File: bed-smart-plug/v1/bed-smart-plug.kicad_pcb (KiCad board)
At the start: 2 copper layers, 122.6 x 80.6 mm, 26 parts, among them J1 DS18b20, J2 Conn_01x02_Male, J3 3.5mm headphone jack, J4 Triac gate protection, J5 Opto snubber, J6 Opto snubber 2, J7 Main, J8 Triac snubber, J9 Prises, Q1 BT136-600E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

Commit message: wip pcb v1
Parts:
- removed AE1: Antenna, Connector_PinHeader_2.54mm:PinHeader_1x01_P2.54mm_Vertical
- removed C1: 47nF/400V, Capacitor_SMD:C_1206_3216Metric
- removed C2: 10nF/400V, Capacitor_SMD:C_0805_2012Metric
- removed D1: LED, Diode_SMD:D_0805_2012Metric
- removed F1: 3A, Fuse:Fuseholder_Cylinder-5x20mm_Schurter_0031_8201_Horizontal_Open
- removed J1: DS18b20, Connector_PinHeader_2.54mm:PinHeader_1x03_P2.54mm_Vertical
- removed J2: Conn_01x02_Male, Connector_PinHeader_2.54mm:PinHeader_1x04_P2.54mm_Vertical
- removed J4: Triac gate protection, Connector_PinHeader_2.54mm:PinHeader_1x02_P2.54mm_Vertical
- removed J5: Opto snubber, Connector_PinHeader_2.54mm:PinHeader_1x03_P2.54mm_Vertical
- removed J6: Opto snubber 2, Connector_PinHeader_2.54mm:PinHeader_1x02_P2.54mm_Vertical
- removed J7: Main, TerminalBlock:TerminalBlock_bornier-2_P5.08mm
- removed J8: Triac snubber, Connector_PinHeader_2.54mm:PinHeader_1x02_P2.54mm_Vertical
- removed J9: Prises, TerminalBlock:TerminalBlock_bornier-2_P5.08mm
- removed PS1: Alim RS PRO 5V 1A, Converter_ACDC:Converter_ACDC_MeanWell_IRM-03-xx_THT
- removed R1: 4.7KΩ, Resistor_SMD:R_0402_1005Metric
- removed R2, R3: 220Ω, Resistor_SMD:R_0603_1608Metric
- removed R4: 360Ω/0.5W, Resistor_SMD:R_1210_3225Metric
- removed R5: 470Ω/0.5W, Resistor_SMD:R_1210_3225Metric
- removed R6: 39Ω/0.5W, Resistor_SMD:R_1210_3225Metric
- removed U2: AM-RX12A-433P, mylife-footprints:AMRX12A433P
- removed U3: MOC3021M, Package_DIP:SMDIP-6_W9.53mm
- added ?: , , F.Cu at (202.0, 57.2)
- added ?: , , F.Cu at (163.5, 83.7)
- added ?: , , F.Cu at (87.2, 57.2)
- added ?: , , F.Cu at (163.5, 55.8)
- added ?: , , F.Cu at (202.0, 111.4)
- moved J3 105.6 mm to (210.3, 78.6), turned to 180 degrees
- moved Q1 55.0 mm to (102.8, 68.5), turned to 90 degrees
- moved HS1 49.3 mm to (99.3, 65.9), turned to 90 degrees
- moved U1 44.3 mm to (179.9, 69.7), turned to 90 degrees
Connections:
- Q1 pad 1: Net-(J8-Pin_2) -> (no net)
- Q1 pad 2: Net-(J5-Pin_3) -> (no net)
- Q1 pad 3: Net-(Q1-G) -> (no net)
- U1 pad 1: +5V -> (no net)
- U1 pad 11: Net-(J1-Pin_3) -> (no net)
- U1 pad 19: Net-(U1-GPIO36) -> (no net)
- U1 pad 2: +3V3 -> (no net)
- U1 pad 3: GND -> (no net)
- U1 pad 7: Net-(U1-GPIO2) -> (no net)
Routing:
- net GND: track 189.9 -> 0.00 mm
- net +3V3: track 134.3 -> 0.00 mm, vias 1 -> 0
- net NEUT: track 97.6 -> 0.00 mm
- net Net-(U1-GPIO2): track 93.8 -> 0.00 mm
- net +5V: track 81.2 -> 0.00 mm
- net Net-(J5-Pin_3): track 78.1 -> 0.00 mm
- net LINE: track 63.4 -> 0.00 mm
- net Net-(J8-Pin_2): track 62.5 -> 0.00 mm
- net Net-(Q1-G): track 47.7 -> 0.00 mm
- net Net-(U1-GPIO36): track 34.1 -> 0.00 mm, vias 1 -> 0
- net Net-(J4-Pin_2): track 32.1 -> 0.00 mm
- net Net-(J4-Pin_1): track 28.5 -> 0.00 mm
- net Net-(J1-Pin_3): track 26.6 -> 0.00 mm
- net Net-(J5-Pin_1): track 21.9 -> 0.00 mm
- net Net-(R3-Pad1): track 20.2 -> 0.00 mm, vias 2 -> 0
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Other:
- board size 122.6 x 80.6 mm -> 145 x 75 mm
- board text removed: "3V3"
- board text removed: "Close x2=ON"
- board text removed: "Close=OFF"
- board text removed: "Close=ON"
- board text removed: "DATA"
- board text removed: "GND"
- board text removed: "Open=ON"

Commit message: wip pcb v1
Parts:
- added AE1: Antenna, Connector_PinHeader_2.54mm:PinHeader_1x01_P2.54mm_Vertical, F.Cu at (126.3, 136.2)
- added D1: LED, Diode_SMD:D_0805_2012Metric, F.Cu at (126.3, 140.1)
- added D2: LED, Diode_SMD:D_0805_2012Metric, F.Cu at (126.3, 143.1)
- added D3: LED, Diode_SMD:D_0805_2012Metric, F.Cu at (126.3, 146.2)
- added D4: LED, Diode_SMD:D_0805_2012Metric, F.Cu at (126.3, 149.2)
- added F1: 3A, Fuse:Fuseholder_Cylinder-5x20mm_Schurter_0031_8201_Horizontal_Open, F.Cu at (189.3, 90.5)
- added HS2: Heatsink (shared by 2 triacs), Heatsink:Heatsink_Fischer_SK104-STC-STIC_35x13mm_2xDrill2.5mm, F.Cu at (79.0, 69.4)
- added J2: Main + Sorties, TerminalBlock:TerminalBlock_bornier-6_P5.08mm, F.Cu at (132.5, 51.2)
- added PS1: Alim RS PRO 5V 1A, Converter_ACDC:Converter_ACDC_MeanWell_IRM-03-xx_THT, F.Cu at (107.9, 54.5)
- added Q2: BT136-600E, Package_TO_SOT_THT:TO-220-3_Vertical, F.Cu at (100.5, 71.8)
- added Q3: BT136-600E, Package_TO_SOT_THT:TO-220-3_Vertical, F.Cu at (113.6, 125.9)
- added Q4: BT136-600E, Package_TO_SOT_THT:TO-220-3_Vertical, F.Cu at (113.6, 131.9)
- added R1: 4.7KΩ, Resistor_SMD:R_0402_1005Metric, F.Cu at (125.5, 151.7)
- added R10: 220Ω, Resistor_SMD:R_0603_1608Metric, F.Cu at (116.4, 140.2)
- added R11: 220Ω, Resistor_SMD:R_0603_1608Metric, F.Cu at (116.4, 142.7)
- added R12: 220Ω, Resistor_SMD:R_0603_1608Metric, F.Cu at (116.4, 145.2)
- added R13: 360Ω/0.5W, Resistor_SMD:R_1210_3225Metric, F.Cu at (121.2, 136.0)
- added R14: 360Ω/0.5W, Resistor_SMD:R_1210_3225Metric, F.Cu at (121.2, 140.2)
- added R15: 360Ω/0.5W, Resistor_SMD:R_1210_3225Metric, F.Cu at (121.2, 144.4)
- added R16: 360Ω/0.5W, Resistor_SMD:R_1210_3225Metric, F.Cu at (121.2, 148.6)
- added R2: 10KΩ, Resistor_SMD:R_0603_1608Metric, F.Cu at (112.4, 135.2)
- added R3: 10KΩ, Resistor_SMD:R_0603_1608Metric, F.Cu at (112.4, 137.7)
- added R4: 10KΩ, Resistor_SMD:R_0603_1608Metric, F.Cu at (112.4, 140.2)
- added R5: 330Ω, Resistor_SMD:R_0603_1608Metric, F.Cu at (112.4, 142.7)
- added R6: 330Ω, Resistor_SMD:R_0603_1608Metric, F.Cu at (112.4, 145.2)
- added R7: 330Ω, Resistor_SMD:R_0603_1608Metric, F.Cu at (112.4, 147.7)
- added R8: 330Ω, Resistor_SMD:R_0603_1608Metric, F.Cu at (116.4, 135.2)
- added R9: 220Ω, Resistor_SMD:R_0603_1608Metric, F.Cu at (116.4, 137.7)
- added U2: QAM-RX10-433, mylife-footprints:AMRX12A433P, F.Cu at (187.6, 51.2)
- added U3: MOC3021M, Package_DIP:SMDIP-6_W9.53mm, F.Cu at (103.8, 120.7)
- added U4: MOC3021M, Package_DIP:SMDIP-6_W9.53mm, F.Cu at (103.8, 129.9)
- added U5: MOC3021M, Package_DIP:SMDIP-6_W9.53mm, F.Cu at (103.8, 139.2)
- added U6: MOC3021M, Package_DIP:SMDIP-6_W9.53mm, F.Cu at (103.8, 148.4)
- HS1: value Heatsink -> Heatsink (shared by 2 triacs)
- moved Q1 9.47 mm to (93.5, 66.8), turned to -90 degrees
- moved HS1 4.12 mm to (97.0, 69.3), turned to -90 degrees
- renumbered J3 to J1
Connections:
- J1 pad R1: Net-(J2-Pin_3) -> Net-(U1-GPIO13)
- J1 pad R2: Net-(J2-Pin_2) -> Net-(U1-GPIO13)
- J1 pad S: Net-(J2-Pin_1) -> GND
- J1 pad T: Net-(J2-Pin_4) -> +3V3
- Q1 pad 1: (no net) -> Net-(J2-Pin_3)
- Q1 pad 2: (no net) -> Net-(Q1-A2)
- Q1 pad 3: (no net) -> Net-(Q1-G)
- U1 pad 1: (no net) -> +5V
- U1 pad 10: unconnected-(U1-GPIO5-Pad10) -> Net-(U1-GPIO5)
- U1 pad 11: (no net) -> Net-(U1-GPIO13)
- U1 pad 19: (no net) -> Net-(U1-GPIO36)
- U1 pad 2: (no net) -> +3V3
- U1 pad 3: (no net) -> GND
- U1 pad 7: (no net) -> Net-(U1-GPIO2)
- U1 pad 8: unconnected-(U1-GPIO3-Pad8) -> Net-(U1-GPIO3)
- U1 pad 9: unconnected-(U1-GPIO4-Pad9) -> Net-(U1-GPIO4)

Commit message: place components
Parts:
- moved Q3 70.3 mm to (75.5, 66.8), turned to -90 degrees
- moved Q4 67.6 mm to (82.4, 71.9), turned to 90 degrees

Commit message: wip placement
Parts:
- moved U6 108.3 mm to (178.1, 69.6), turned to 90 degrees
- moved R1 104.6 mm to (201.1, 79.5), turned to 90 degrees
- moved AE1 95.5 mm to (164.1, 48.5)
- moved U5 93.5 mm to (166.3, 69.6), turned to 90 degrees
- moved U4 79.1 mm to (154.9, 69.5), turned to 90 degrees
- moved D4 67.9 mm to (156.8, 88.6)
- moved U3 65.2 mm to (144.3, 69.5), turned to 90 degrees
- moved D3 63.1 mm to (152.0, 88.6)
- moved D2 59.2 mm to (146.1, 87.3), turned to 90 degrees
- moved D1 55.1 mm to (142.2, 87.3), turned to 90 degrees
- moved R13 48.0 mm to (148.3, 96.4)
- moved R14 42.6 mm to (133.2, 99.3)
- moved R2 42.3 mm to (150.1, 116.1)
- moved R3 42.3 mm to (150.1, 118.6)
- moved R4 42.3 mm to (150.1, 121.1)
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
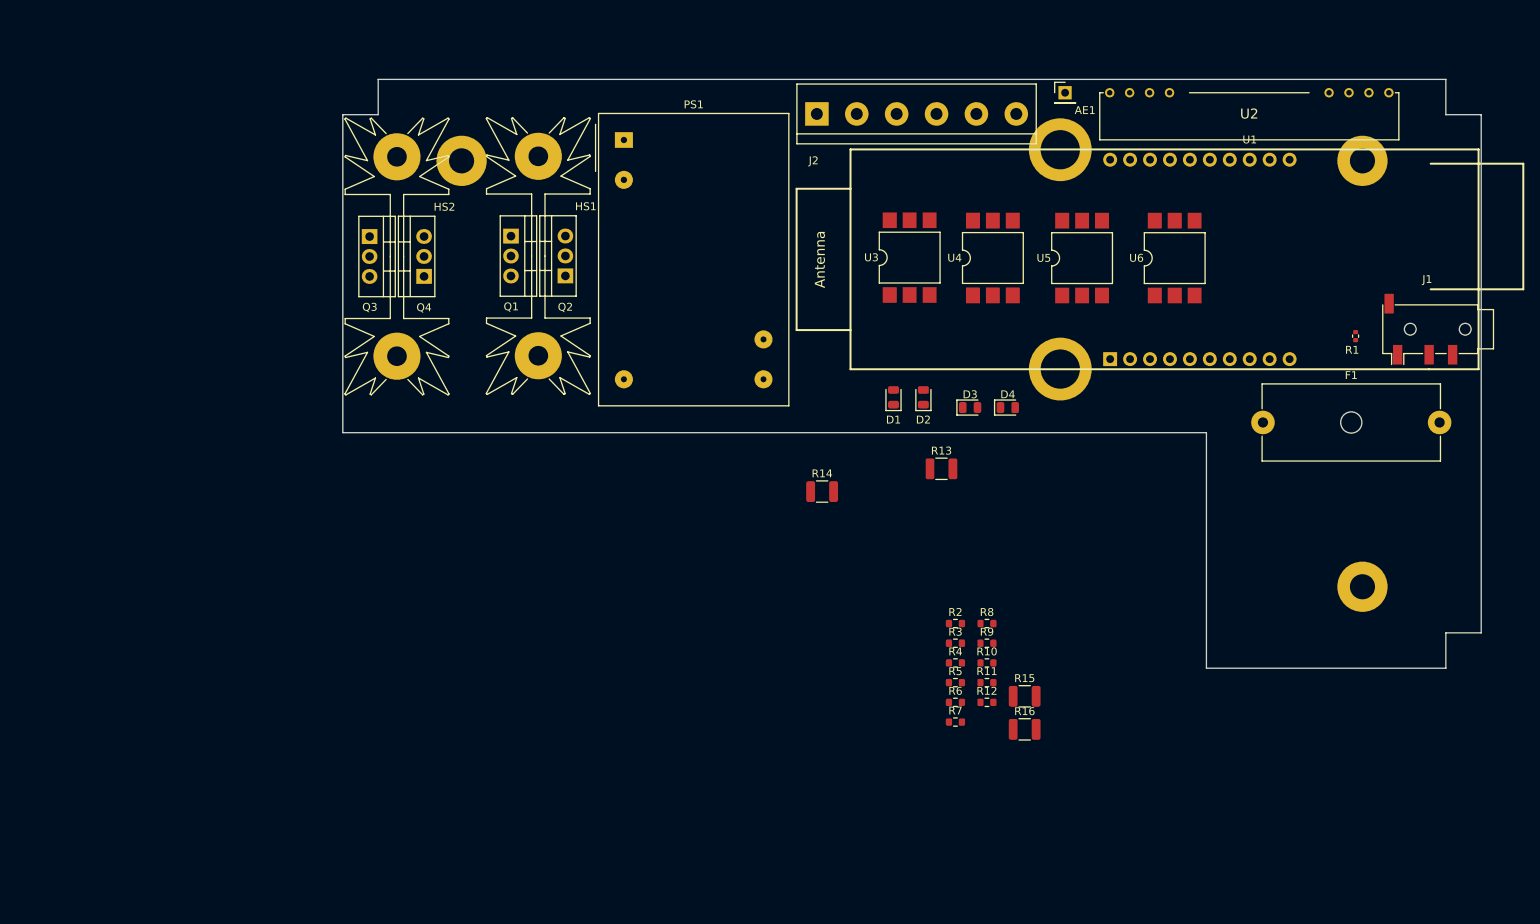
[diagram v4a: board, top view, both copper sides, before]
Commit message: component placement
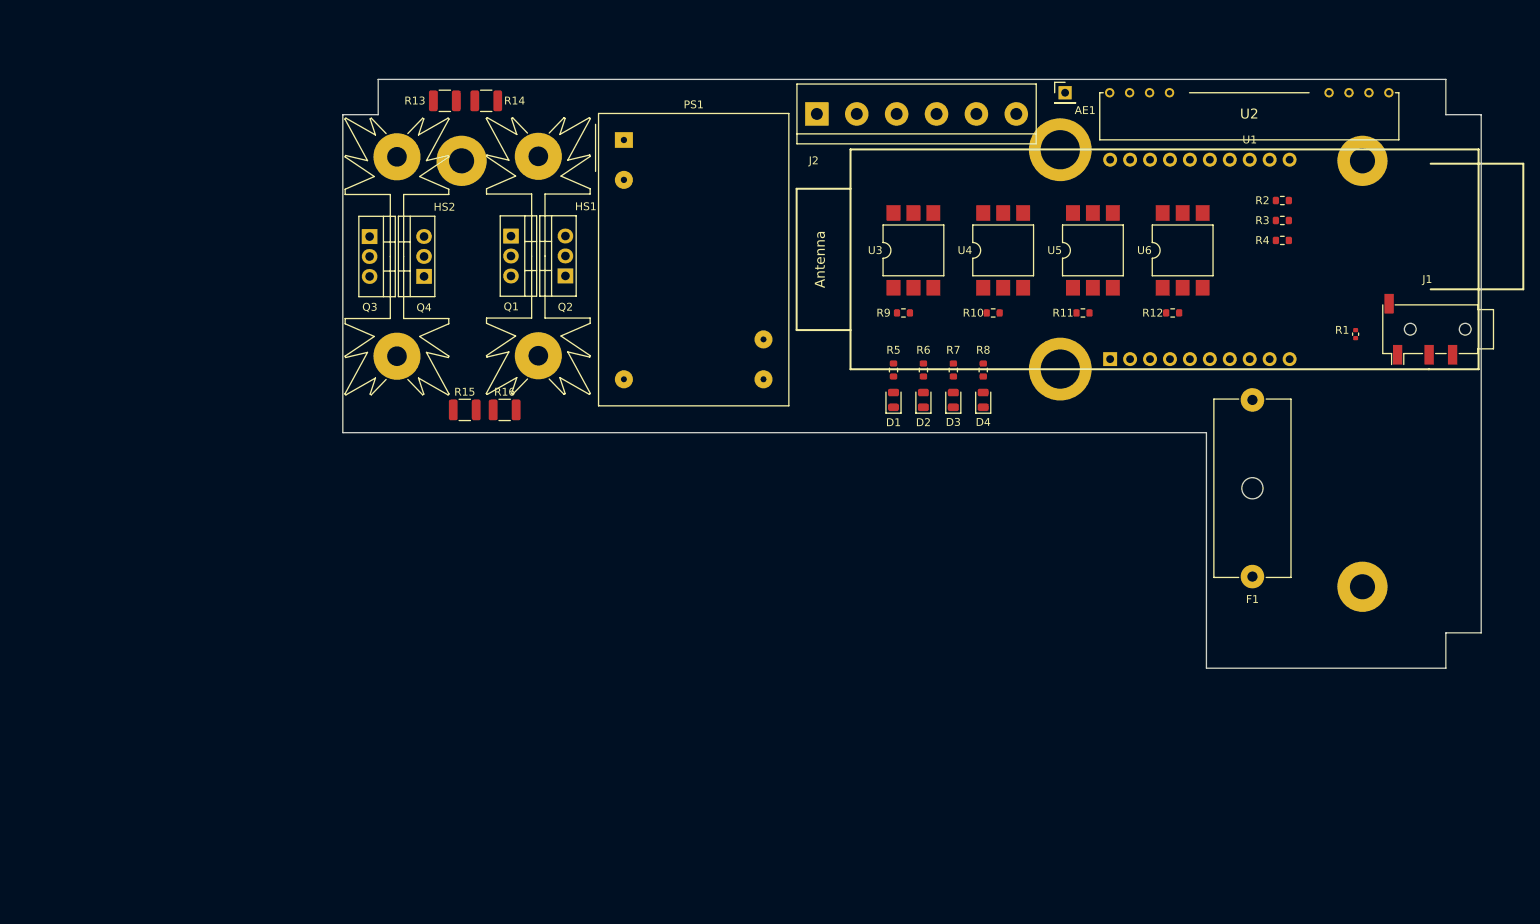
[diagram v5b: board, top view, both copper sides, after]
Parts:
- moved R15 80.1 mm to (87.6, 88.9)
- moved R13 78.7 mm to (85.1, 49.5), turned to 180 degrees
- moved R16 77.7 mm to (92.7, 88.9)
- moved R2 68.1 mm to (191.8, 62.2)
- moved R3 68.1 mm to (191.8, 64.8)
- moved R4 68.0 mm to (191.8, 67.3)
- moved R14 65.6 mm to (90.4, 49.5)
- moved R12 55.0 mm to (177.8, 76.5)
- moved R11 48.7 mm to (166.4, 76.5)
- moved R7 44.8 mm to (149.9, 83.8), turned to -90 degrees
- moved R10 44.6 mm to (154.9, 76.5)
- moved R9 43.4 mm to (143.5, 76.5)
- moved R6 42.5 mm to (146.1, 83.8), turned to -90 degrees
- moved R5 40.6 mm to (142.2, 83.8), turned to -90 degrees
- moved R8 32.3 mm to (153.7, 83.8), turned to -90 degrees
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
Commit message: pcb
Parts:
- moved R16 87.1 mm to (176.5, 65.4), turned to 90 degrees
- moved R15 79.7 mm to (163.8, 65.4), turned to 90 degrees
- moved R14 62.8 mm to (151.1, 65.4), turned to 90 degrees
- moved R13 55.7 mm to (138.4, 65.4), turned to 90 degrees
- moved R12 3.81 mm to (181.6, 76.5)
- moved U6 3.81 mm to (182.9, 68.6)
- moved U5 2.54 mm to (170.2, 68.6)
- moved R11 2.54 mm to (168.9, 76.5)
- moved R10 1.27 mm to (156.2, 76.5)
- moved U4 1.27 mm to (157.5, 68.6)
- renumbered HS2 to HS1, HS1 to HS2, Q3 to Q1, Q4 to Q2, Q1 to Q3, Q2 to Q4
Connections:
- Q1 pad 1: Net-(J2-Pin_5) -> Net-(J2-Pin_3)
- Q1 pad 3: Net-(Q3-G) -> Net-(Q1-G)
- Q2 pad 1: Net-(J2-Pin_6) -> Net-(J2-Pin_4)
- Q2 pad 3: Net-(Q4-G) -> Net-(Q2-G)
- Q3 pad 1: Net-(J2-Pin_3) -> Net-(J2-Pin_5)
- Q3 pad 3: Net-(Q1-G) -> Net-(Q3-G)
- Q4 pad 1: Net-(J2-Pin_4) -> Net-(J2-Pin_6)
- Q4 pad 3: Net-(Q2-G) -> Net-(Q4-G)
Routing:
- net GND: track 0.00 -> 198.5 mm, vias 0 -> 3
- net Net-(Q1-A2): track 0.00 -> 194.8 mm, vias 0 -> 1
- net LINE: track 0.00 -> 149.0 mm
- net +3V3: track 0.00 -> 88.9 mm, vias 0 -> 2
- net Net-(J2-Pin_4): track 0.00 -> 75.5 mm
- net Net-(J2-Pin_3): track 0.00 -> 74.7 mm
- net Net-(J2-Pin_5): track 0.00 -> 67.1 mm
- net Net-(J2-Pin_6): track 0.00 -> 66.0 mm
- net +5V: track 0.00 -> 54.1 mm
- net NEUT: track 0.00 -> 43.9 mm
- net Net-(U1-GPIO13): track 0.00 -> 41.1 mm, vias 0 -> 1
- net Net-(U1-GPIO5): track 0.00 -> 28.8 mm
- net Net-(U1-GPIO36): track 0.00 -> 24.6 mm
- net Net-(U1-GPIO4): track 0.00 -> 20.0 mm
- net Net-(R2-Pad2): track 0.00 -> 19.4 mm
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
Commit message: wip routing
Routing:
- net Net-(Q4-G): track 0.00 -> 99.0 mm
- net Net-(Q2-G): track 0.00 -> 98.1 mm, vias 0 -> 4
- net Net-(Q3-G): track 0.00 -> 90.2 mm, vias 0 -> 4
- net Net-(Q1-G): track 0.00 -> 84.8 mm, vias 0 -> 4
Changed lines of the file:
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@@
   (segment (start 192.695 68.235) (end 193.04 68.58) (width 0.25) (layer "B.Cu") (net 12))
   (segment (start 192.695 57.03) (end 192.695 68.235) (width 0.25) (layer "B.Cu") (net 12))
+  (segment (start 127 74.295) (end 125.095 76.2) (width 0.25) (layer "F.Cu") (net 13))
+  (segment (start 160.02 63.815) (end 160.02 66.04) (width 0.25) (layer "F.Cu") (net 13))
+  (segment (start 79.375 72.39) (end 79.375 69.88) (width 0.25) (layer "F.Cu") (net 13))
+  (segment (start 83.185 76.2) (end 79.375 72.39) (width 0.25) (layer "F.Cu") (net 13))
+  (segment (start 125.095 76.2) (end 83.185 76.2) (width 0.25) (layer "F.Cu") (net 13))
+  (segment (start 131.445 69.85) (end 127 69.85) (width 0.25) (layer "F.Cu") (net 13))
+  (segment (start 79.375 69.88) (end 82.445 66.81) (width 0.25) (layer "F.Cu") (net 13))
+  (segment (start 127 73.66) (end 127 74.295) (width 0.25) (layer "F.Cu") (net 13))
+  (segment (start 135.89 69.85) (end 131.445 69.85) (width 0.25) (layer "F.Cu") (net 13))
+  (via (at 135.89 69.85) (size 0.8) (drill 0.4) (layers "F.Cu" "B.Cu") (net 13))
+  (via (at 127 73.66) (size 0.8) (drill 0.4) (layers "F.Cu" "B.Cu") (net 13))
+  (via (at 127 69.85) (size 0.8) (drill 0.4) (layers "F.Cu" "B.Cu") (net 13))
+  (via (at 160.02 66.04) (size 0.8) (drill 0.4) (layers "F.Cu" "B.Cu") (net 13))
+  (segment (start 156.21 69.85) (end 137.795 69.85) (width 0.25) (layer "B.Cu") (net 13))
+  (segment (start 160.02 66.04) (end 156.21 69.85) (width 0.25) (layer "B.Cu") (net 13))
+  (segment (start 137.795 69.85) (end 135.89 69.85) (width 0.25) (layer "B.Cu") (net 13))
+  (segment (start 127 69.85) (end 127 73.66) (width 0.25) (layer "B.Cu") (net 13))
   (segment (start 105.41 57.11) (end 105.41 51.435) (width 0.25) (layer "F.Cu") (net 14))
   (segment (start 134.62 48.26) (end 137.56 51.2) (width 0.25) (layer "F.Cu") (net 14))
@@
   (segment (start 133.35 87.63) (end 125.68 79.96) (width 0.25) (layer "F.Cu") (net 16))
   (segment (start 169.835 86.705) (end 166.37 90.17) (width 0.25) (layer "F.Cu") (net 16))
+  (segment (start 128.27 74.93) (end 125.73 77.47) (width 0.25) (layer "F.Cu") (net 17))
+  (segment (start 147.32 63.815) (end 147.32 66.04) (width 0.25) (layer "F.Cu") (net 17))
+  (segment (start 130.175 68.58) (end 128.27 68.58) (width 0.25) (layer "F.Cu") (net 17))
+  (segment (start 125.73 77.47) (end 102.87 77.47) (width 0.25) (layer "F.Cu") (net 17))
+  (segment (start 128.27 73.66) (end 128.27 74.93) (width 0.25) (layer "F.Cu") (net 17))
+  (segment (start 75.51 71.9) (end 81.08 77.47) (width 0.25) (layer "F.Cu") (net 17))
+  (segment (start 81.08 77.47) (end 102.87 77.47) (width 0.25) (layer "F.Cu") (net 17))
+  (segment (start 134.62 68.58) (end 130.175 68.58) (width 0.25) (layer "F.Cu") (net 17))
+  (via (at 134.62 68.58) (size 0.8) (drill 0.4) (layers "F.Cu" "B.Cu") (net 17))
+  (via (at 128.27 73.66) (size 0.8) (drill 0.4) (layers "F.Cu" "B.Cu") (net 17))
+  (via (at 128.27 68.58) (size 0.8) (drill 0.4) (layers "F.Cu" "B.Cu") (net 17))
+  (via (at 147.32 66.04) (size 0.8) (drill 0.4) (layers "F.Cu" "B.Cu") (net 17))
+  (segment (start 137.795 68.58) (end 134.62 68.58) (width 0.25) (layer "B.Cu") (net 17))
+  (segment (start 147.32 66.04) (end 144.78 68.58) (width 0.25) (layer "B.Cu") (net 17))
+  (segment (start 144.78 68.58) (end 137.795 68.58) (width 0.25) (layer "B.Cu") (net 17))
+  (segment (start 128.27 68.58) (end 128.27 73.66) (width 0.25) (layer "B.Cu") (net 17))
   (segment (start 142.24 82.995) (end 144.335 80.9) (width 0.25) (layer "F.Cu") (net 18))
   (segment (start 144.335 80.9) (end 144.335 76.55) (width 0.25) (layer "F.Cu") (net 18))
+  (segment (start 132.715 71.12) (end 125.73 71.12) (width 0.25) (layer "F.Cu") (net 22))
+  (segment (start 136.525 71.12) (end 132.715 71.12) (width 0.25) (layer "F.Cu") (net 22))
+  (segment (start 93.515 73.195) (end 93.515 71.84) (width 0.25) (layer "F.Cu") (net 22))
+  (segment (start 139.065 68.58) (end 136.525 71.12) (width 0.25) (layer "F.Cu") (net 22))
+  (segment (start 95.25 74.93) (end 93.515 73.195) (width 0.25) (layer "F.Cu") (net 22))
+  (segment (start 125.73 73.66) (end 124.46 74.93) (width 0.25) (layer "F.Cu") (net 22))
+  (segment (start 172.72 63.815) (end 172.72 66.04) (width 0.25) (layer "F.Cu") (net 22))
+  (segment (start 172.72 68.58) (end 148.59 68.58) (width 0.25) (layer "F.Cu") (net 22))
+  (segment (start 124.46 74.93) (end 95.25 74.93) (width 0.25) (layer "F.Cu") (net 22))
+  (segment (start 148.59 68.58) (end 139.065 68.58) (width 0.25) (layer "F.Cu") (net 22))
+  (via (at 125.73 73.66) (size 0.8) (drill 0.4) (layers "F.Cu" "B.Cu") (net 22))
+  (via (at 172.72 66.04) (size 0.8) (drill 0.4) (layers "F.Cu" "B.Cu") (net 22))
+  (via (at 172.72 68.58) (size 0.8) (drill 0.4) (layers "F.Cu" "B.Cu") (net 22))
+  (via (at 125.73 71.12) (size 0.8) (drill 0.4) (layers "F.Cu" "B.Cu") (net 22))
+  (segment (start 172.72 66.04) (end 172.72 68.58) (width 0.25) (layer "B.Cu") (net 22))
+  (segment (start 125.73 71.12) (end 125.73 73.66) (width 0.25) (layer "B.Cu") (net 22))
+  (segment (start 99.06 73.66) (end 97.79 72.39) (width 0.25) (layer "F.Cu") (net 23))
+  (segment (start 137.16 72.39) (end 125.095 72.39) (width 0.25) (layer "F.Cu") (net 23))
+  (segment (start 125.095 72.39) (end 123.825 73.66) (width 0.25) (layer "F.Cu") (net 23))
+  (segment (start 97.79 72.39) (end 97.79 69.41) (width 0.25) (layer "F.Cu") (net 23))
+  (segment (start 123.825 73.66) (end 99.06 73.66) (width 0.25) (layer "F.Cu") (net 23))
+  (segment (start 139.7 69.85) (end 137.16 72.39) (width 0.25) (layer "F.Cu") (net 23))
+  (segment (start 185.42 63.815) (end 179.385 69.85) (width 0.25) (layer "F.Cu") (net 23))
+  (segment (start 179.385 69.85) (end 139.7 69.85) (width 0.25) (layer "F.Cu") (net 23))
+  (segment (start 97.79 69.41) (end 100.45 66.75) (width 0.25) (layer "F.Cu") (net 23))
   (segment (start 172.375 57.03) (end 172.375 59.345) (width 0.25) (layer "F.Cu") (net 31))
   (segment (start 189.675 60.96) (end 190.945 62.23) (width 0.25) (layer "F.Cu") (net 31))

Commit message: pcb ok
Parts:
- moved R10 0.98 mm to (156.2, 75.6)
- moved R11 0.98 mm to (168.9, 75.6)
- moved R12 0.98 mm to (181.6, 75.6)
- moved R9 0.98 mm to (143.5, 75.6)
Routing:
- net Net-(U1-GPIO2): track 7.31 -> 53.1 mm, vias 0 -> 1
- net Net-(U1-GPIO3): track 13.4 -> 49.0 mm, vias 0 -> 1
- net Net-(U1-GPIO4): track 20.0 -> 47.5 mm, vias 0 -> 1
- net Net-(U1-GPIO5): track 28.8 -> 46.5 mm, vias 0 -> 1
- net GND: track 198.5 -> 211.5 mm
- net +5V: track 54.1 -> 48.3 mm
- net LINE: track 149.0 -> 145.6 mm
- net Net-(J2-Pin_3): track 74.7 -> 75.7 mm, vias 0 -> 1
- net Net-(J2-Pin_5): track 67.1 -> 68.1 mm, vias 0 -> 1
- net Net-(J2-Pin_4): track 75.5 -> 74.5 mm
- net Net-(R9-Pad1): track 3.39 -> 2.40 mm
- net Net-(R12-Pad1): track 3.39 -> 2.40 mm
- net Net-(R11-Pad1): track 3.39 -> 2.40 mm
- net Net-(R10-Pad1): track 3.39 -> 2.40 mm
